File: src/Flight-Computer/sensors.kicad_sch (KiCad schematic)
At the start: 30 parts, among them P5 440054-3, P6 440054-3, P7 440054-3, P9 440054-3, Q3 QS5U17TR, Q4 QS5U17TR, Q5 QS5U17TR, Q6 QS5U17TR, U11 BMP390, U8 MPU-9250, U9 MAX-8C-0-10

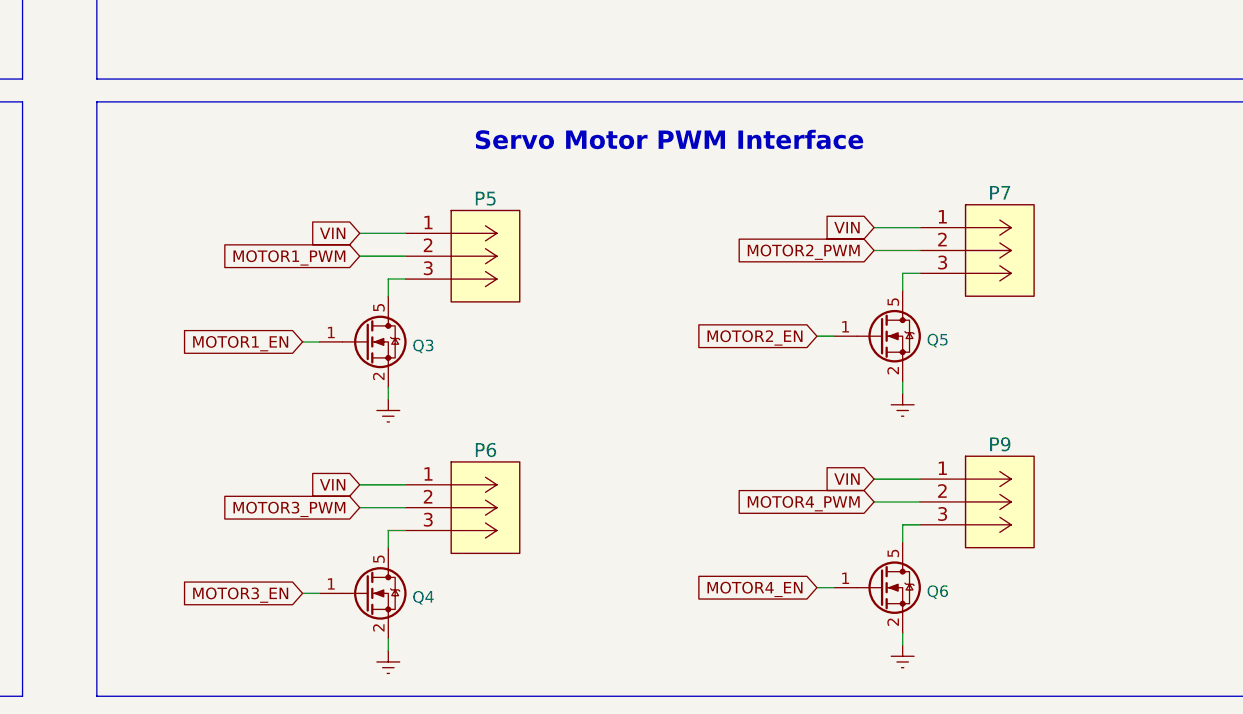
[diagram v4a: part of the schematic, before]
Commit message: implemented pwm motor interface in schematic
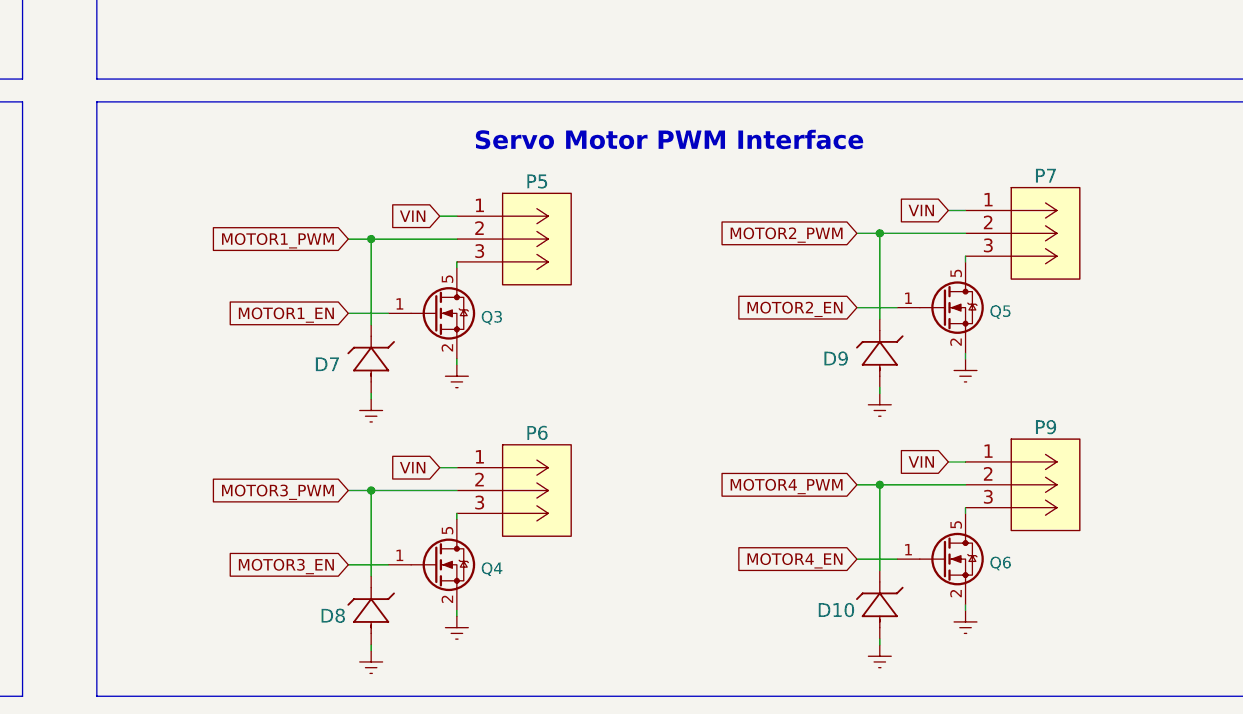
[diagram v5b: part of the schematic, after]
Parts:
- added D10, D7, D8, D9: MM3Z3V3B, symbol Flight-Computer:MM3Z3V3B
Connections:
- net Earth: now also D10.2, D7.2, D8.2, D9.2
- net MOTOR1_PWM: now also D7.1
- net MOTOR2_PWM: now also D9.1
- net MOTOR3_PWM: now also D8.1
- net MOTOR4_PWM: now also D10.1
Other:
- moved on the sheet: P5, Q3
